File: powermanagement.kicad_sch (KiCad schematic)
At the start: 28 parts, among them J1 Battery, Q2 AP2302B, SW6 SW_SPDT, U1 SY8079AAC, U2 XT4054K421MR-G, U3 SY6280AAC

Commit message: Small fixes and change footprint library for missing libraries
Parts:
- added C3: 470n, Capacitor_SMD:C_0805_2012Metric, symbol symbols:C
- D1: footprint tanoshii:D_SOD-323 -> hh24:D_SOD-323
- J5: renamed from J1; footprint tanoshii:JST_S2B-ZR-SM4A-TF(LF)(SN) -> hh24:JST_S2B-ZR-SM4A-TF(LF)(SN)
- L1: footprint tanoshii:Inductor_MSC20FC -> hh24:Inductor_MSC20FC
- Q1: renamed from Q2; footprint tanoshii:SOT-23 -> hh24:SOT-23
- U2: renamed from U1; footprint tanoshii:SOT-23-5 -> hh24:SOT-23-5
- U3: renamed from U2; footprint tanoshii:SOT-23-5 -> hh24:SOT-23-5
- U4: renamed from U3; footprint tanoshii:SOT-23-5 -> hh24:SOT-23-5
- renumbered C6 to C10, C8 to C11, C7 to C12, C3 to C5, C4 to C6, C1 to C7, C5 to C8, C2 to C9, R5 to R11, R6 to R12, R3 to R13, R7 to R14, R11 to R15, R12 to R16, R8 to R17, R13 to R18, R13 to R19, R14 to R20, R8 to R31
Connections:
- net GND: now also C3.1
- net at Q1.3 (D), R17.2, U4.4 (ON): now also C3.2
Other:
- company: Nicolai Electronics -> Nicolai Electronics & tilde.industries
- moved on the sheet: R31

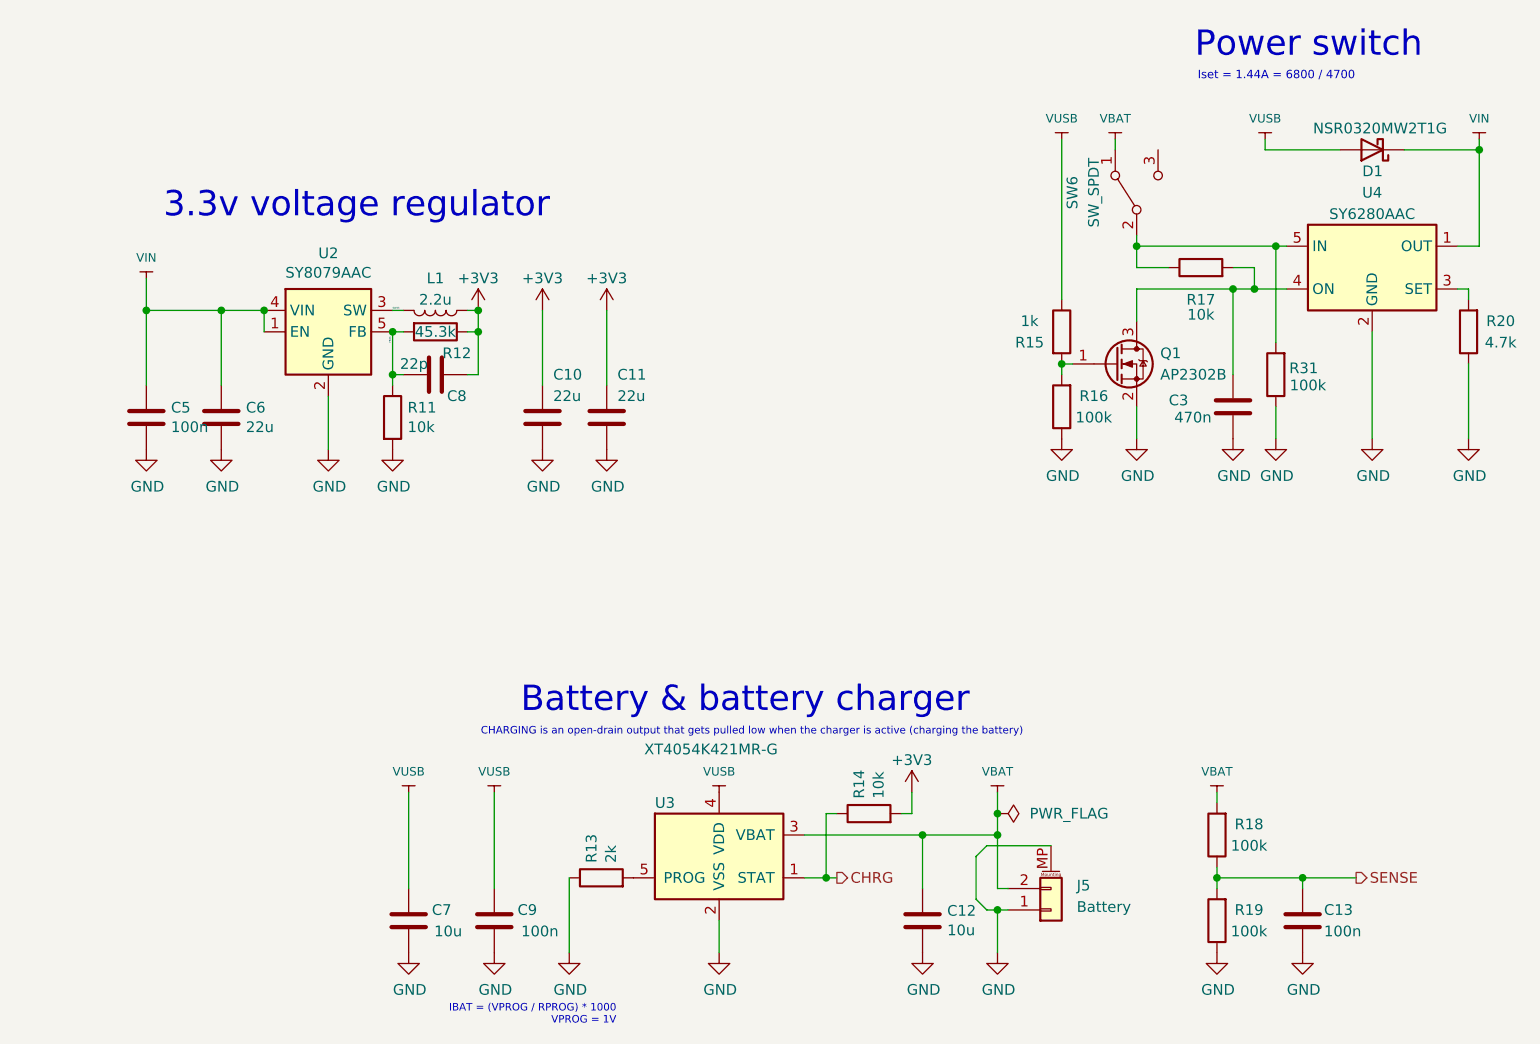
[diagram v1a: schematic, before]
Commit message: Fix power circuit, add headers and move stuff
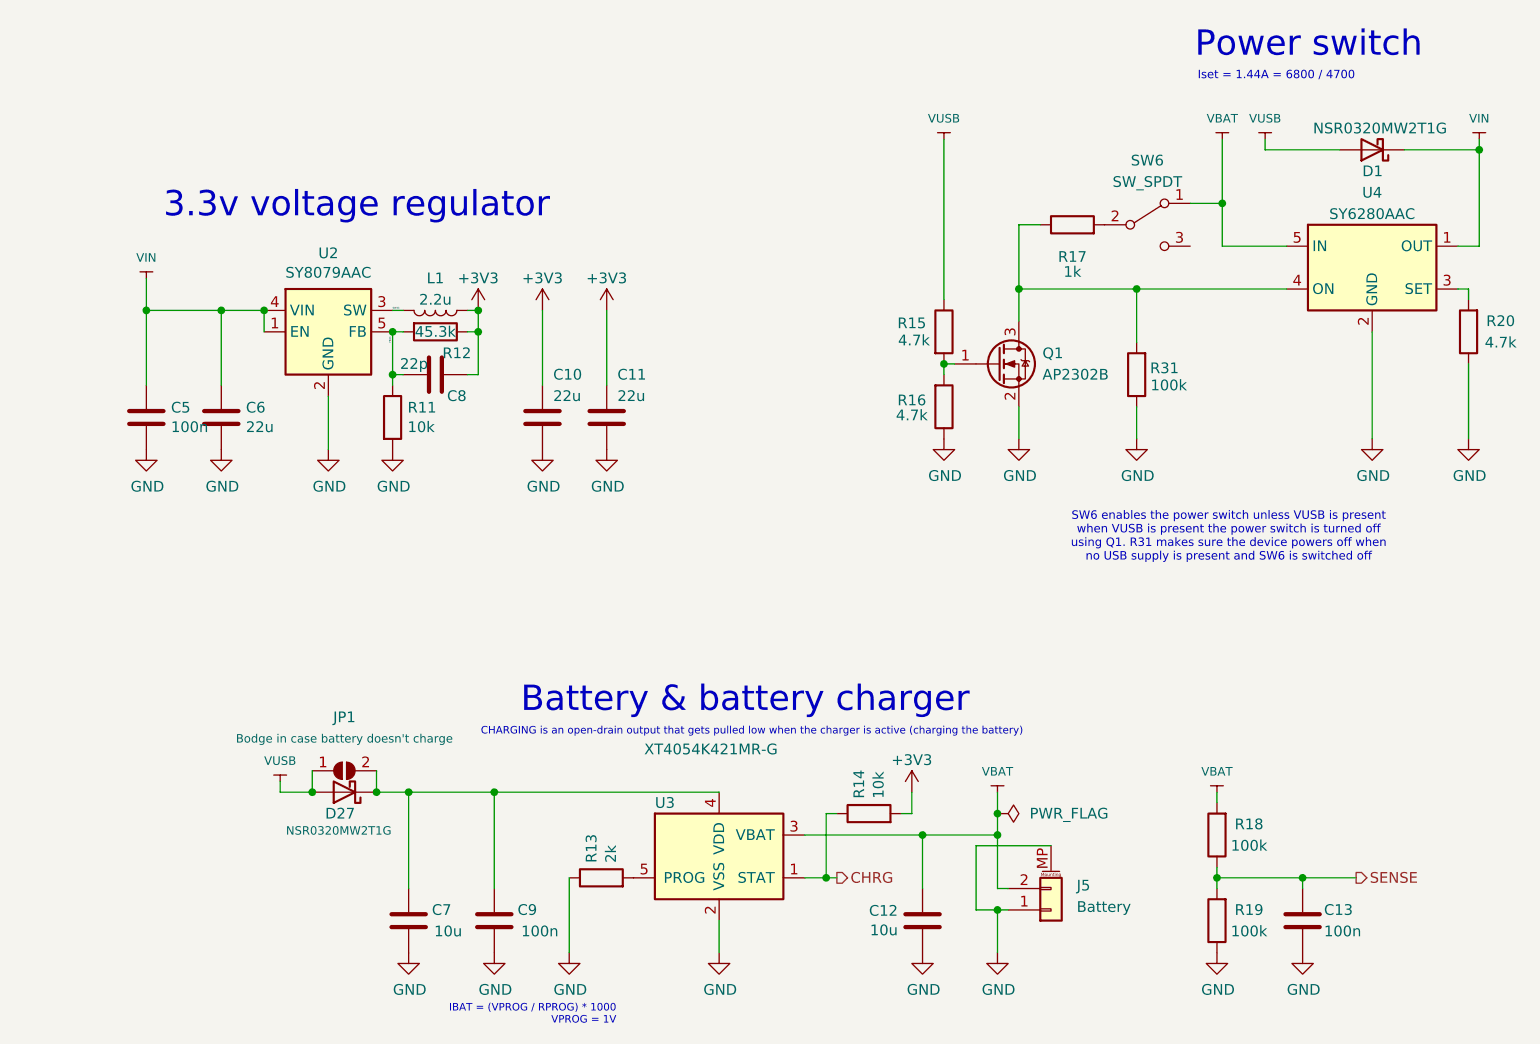
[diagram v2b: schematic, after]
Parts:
- removed C3: 470n, Capacitor_SMD:C_0805_2012Metric, symbol symbols:C
- added D27: NSR0320MW2T1G, hh24:D_SOD-323, symbol symbols:D_Schottky
- added JP1: Bodge in case battery doesn't charge, Jumper:SolderJumper-2_P1.3mm_Open_RoundedPad1.0x1.5mm, symbol Jumper:SolderJumper_2_Open
- R11, R14: LCSC C5140188 -> C5140188
- R15: value 1k -> 4.7k; LCSC C3017842 -> C2907326; Link https://www.lcsc.com/product-detail/Chip-span-style-background-color-ff0-Resistor-span-Surface-Mount_VO-SCR0805J1K_C3017842.html -> https://www.lcsc.com/product-detail/Chip-span-style-background-color-ff0-Resistor-span-Surface-Mount_FOJAN-FRC0805J472-TS_C2907326.html
- R16: value 100k -> 4.7k; LCSC C2907293 -> C2907326; Link https://www.lcsc.com/product-detail/Chip-span-style-background-color-ff0-Resistor-span-Surface-Mount_FOJAN-FRC0805J104-TS_C2907293.html -> https://www.lcsc.com/product-detail/Chip-span-style-background-color-ff0-Resistor-span-Surface-Mount_FOJAN-FRC0805J472-TS_C2907326.html
- R17: value 10k -> 1k; LCSC C5140188 -> C3017842; Link https://www.lcsc.com/product-detail/Chip-span-style-background-color-ff0-Resistor-span-Surface-Mount_VO-SCR0805J10K_C5140188.html -> https://www.lcsc.com/product-detail/Chip-span-style-background-color-ff0-Resistor-span-Surface-Mount_VO-SCR0805J1K_C3017842.html
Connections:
- net VBAT: now also U4.5 (IN)
- net VUSB: now also D27.2 (A), JP1.1 (A); no longer C7.2, C9.2, U3.4 (VDD)
- net at Q1.3 (D), U4.4 (ON): now also R17.1, R31.2; no longer R17.2
- new net: C7.2, C9.2, D27.1 (K), JP1.2 (B), U3.4 (VDD)
- new net: R17.2, SW6.2 (B)
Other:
- note added: "SW6 enables the power switch unless VUSB is present when VUSB is present the power switch is turned off using Q1. R31 makes sure the device powers off when no USB supply is present and SW6 is switched off"
- moved on the sheet: Q1, R15, R16, R17, R31, SW6

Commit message: Moar headers
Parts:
- renumbered C11 to C10, C12 to C11, C13 to C12, C5 to C4, C6 to C5, C7 to C6, C8 to C7, C9 to C8, C10 to C9, D27 to D23, D1 to D24, J5 to J9, Q1 to Q2, R11 to R23, R12 to R24, R13 to R25, R14 to R26, R15 to R27, R16 to R28, R17 to R29, R31 to R30, R18 to R31, R19 to R32, R20 to R33, U2 to U4, U3 to U5, U4 to U6
